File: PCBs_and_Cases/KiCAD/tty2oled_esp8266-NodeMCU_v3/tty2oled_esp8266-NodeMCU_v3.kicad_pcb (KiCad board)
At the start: 2 copper layers, 35.6 x 99.7 mm, 2 parts

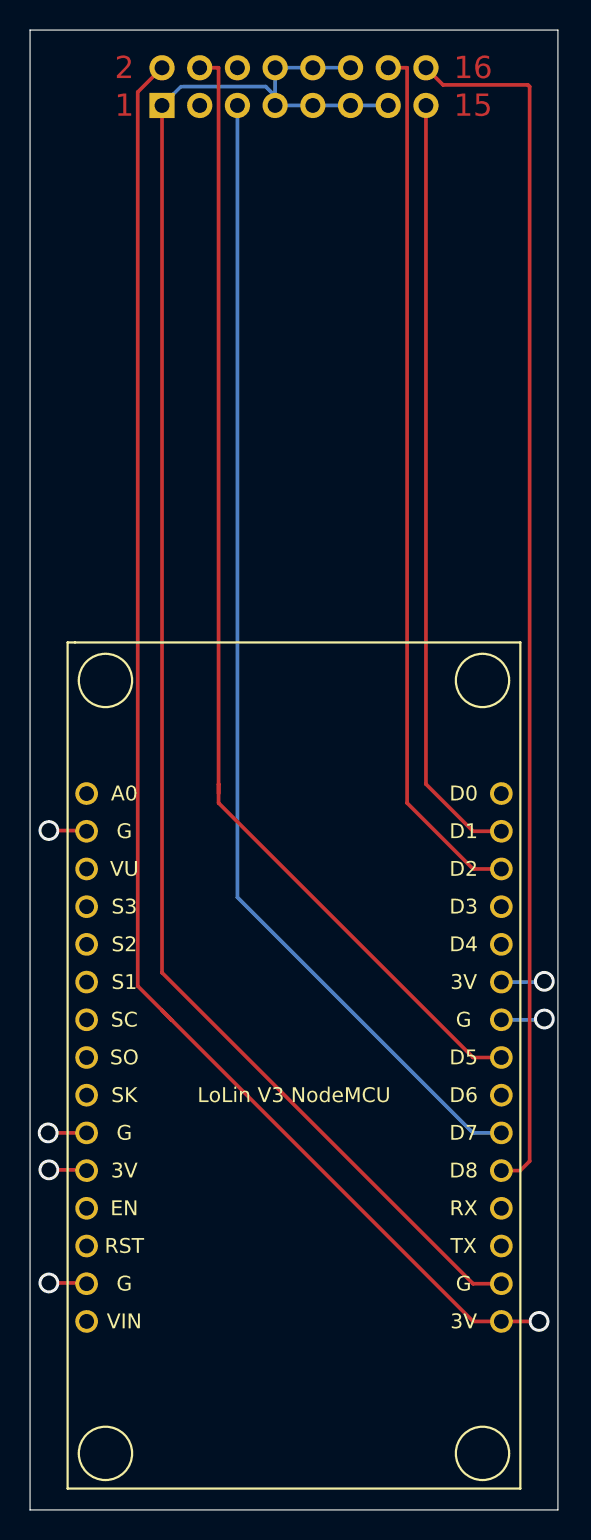
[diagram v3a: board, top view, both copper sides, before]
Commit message: Silkscreen fixed
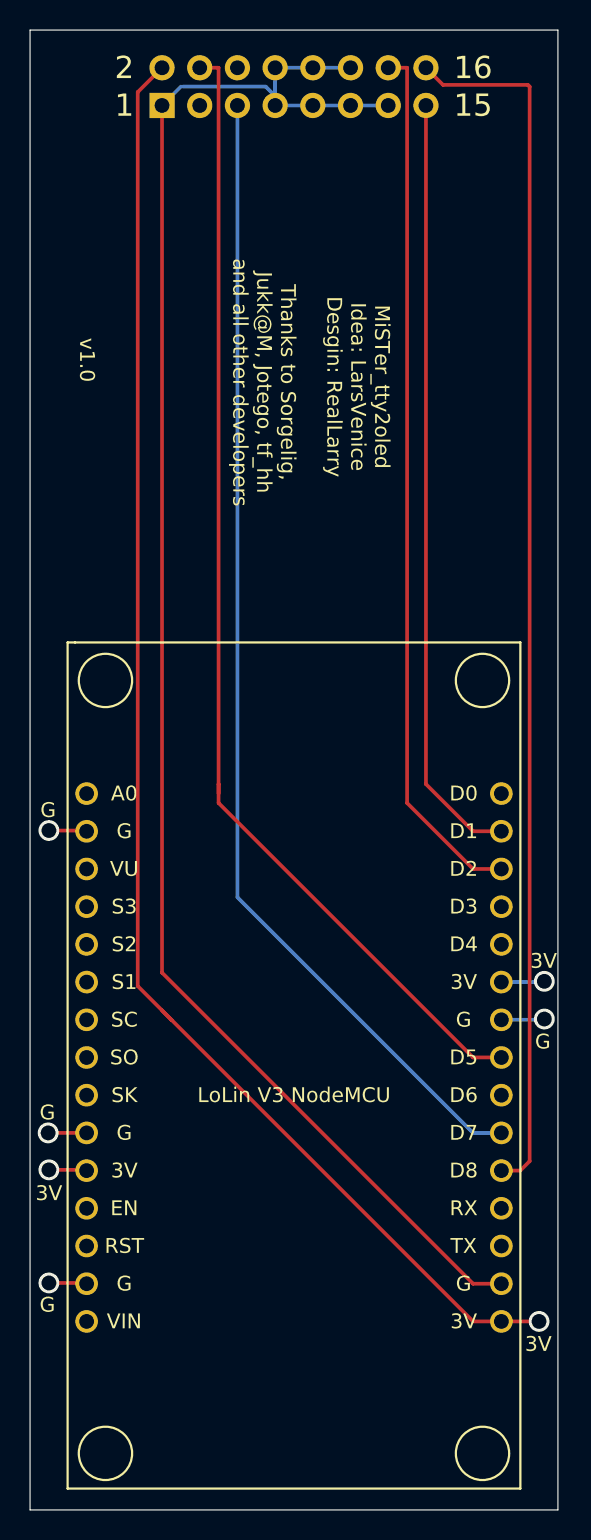
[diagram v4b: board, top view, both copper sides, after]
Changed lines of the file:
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@@
       (effects (font (size 1 1) (thickness 0.15)))
     )
+    (fp_circle (center 12.7 24.13) (end 13.97 22.86) (layer F.SilkS) (width 0.15))
+    (fp_circle (center -12.7 24.13) (end -11.43 22.86) (layer F.SilkS) (width 0.15))
+    (fp_circle (center -12.7 -27.94) (end -11.43 -29.21) (layer F.SilkS) (width 0.15))
+    (fp_circle (center 12.7 -27.94) (end 13.97 -29.21) (layer F.SilkS) (width 0.15))
+    (fp_line (start 15.25 -30.5) (end -14.75 -30.5) (layer F.SilkS) (width 0.15))
+    (fp_line (start -14.75 -30.5) (end -15.25 -30.5) (layer F.SilkS) (width 0.15))
+    (fp_line (start -15.25 -30.5) (end -15.25 26.5) (layer F.SilkS) (width 0.15))
+    (fp_line (start -15.25 26.5) (end 15.25 26.5) (layer F.SilkS) (width 0.15))
     (fp_line (start 15.25 26.5) (end 15.25 -30.5) (layer F.SilkS) (width 0.15))
-    (fp_line (start -15.25 26.5) (end 15.25 26.5) (layer F.SilkS) (width 0.15))
-    (fp_line (start -15.25 -30.5) (end -15.25 26.5) (layer F.SilkS) (width 0.15))
-    (fp_line (start -14.75 -30.5) (end -15.25 -30.5) (layer F.SilkS) (width 0.15))
-    (fp_line (start 15.25 -30.5) (end -14.75 -30.5) (layer F.SilkS) (width 0.15))
-    (fp_circle (center 12.7 -27.94) (end 13.97 -29.21) (layer F.SilkS) (width 0.15))
-    (fp_circle (center -12.7 -27.94) (end -11.43 -29.21) (layer F.SilkS) (width 0.15))
-    (fp_circle (center -12.7 24.13) (end -11.43 22.86) (layer F.SilkS) (width 0.15))
-    (fp_circle (center 12.7 24.13) (end 13.97 22.86) (layer F.SilkS) (width 0.15))
     (fp_text user D0 (at 11.43 -20.32) (layer F.SilkS)
       (effects (font (size 1 1) (thickness 0.15)))
@@
       (effects (font (size 1 1) (thickness 0.15)) (justify mirror))
     )
+    (fp_line (start 4.35 1.8) (end -1.8 1.8) (layer B.CrtYd) (width 0.05))
+    (fp_line (start 4.35 -19.55) (end 4.35 1.8) (layer B.CrtYd) (width 0.05))
+    (fp_line (start -1.8 -19.55) (end 4.35 -19.55) (layer B.CrtYd) (width 0.05))
+    (fp_line (start -1.8 1.8) (end -1.8 -19.55) (layer B.CrtYd) (width 0.05))
+    (fp_line (start -1.33 1.33) (end 0 1.33) (layer B.SilkS) (width 0.12))
+    (fp_line (start -1.33 0) (end -1.33 1.33) (layer B.SilkS) (width 0.12))
+    (fp_line (start 1.27 1.33) (end 3.87 1.33) (layer B.SilkS) (width 0.12))
+    (fp_line (start 1.27 -1.27) (end 1.27 1.33) (layer B.SilkS) (width 0.12))
+    (fp_line (start -1.33 -1.27) (end 1.27 -1.27) (layer B.SilkS) (width 0.12))
+    (fp_line (start 3.87 1.33) (end 3.87 -19.11) (layer B.SilkS) (width 0.12))
+    (fp_line (start -1.33 -1.27) (end -1.33 -19.11) (layer B.SilkS) (width 0.12))
+    (fp_line (start -1.33 -19.11) (end 3.87 -19.11) (layer B.SilkS) (width 0.12))
+    (fp_line (start -1.27 0) (end 0 1.27) (layer B.Fab) (width 0.1))
+    (fp_line (start -1.27 -19.05) (end -1.27 0) (layer B.Fab) (width 0.1))
+    (fp_line (start 3.81 -19.05) (end -1.27 -19.05) (layer B.Fab) (width 0.1))
+    (fp_line (start 3.81 1.27) (end 3.81 -19.05) (layer B.Fab) (width 0.1))
     (fp_line (start 0 1.27) (end 3.81 1.27) (layer B.Fab) (width 0.1))
-    (fp_line (start 3.81 1.27) (end 3.81 -19.05) (layer B.Fab) (width 0.1))
-    (fp_line (start 3.81 -19.05) (end -1.27 -19.05) (layer B.Fab) (width 0.1))
-    (fp_line (start -1.27 -19.05) (end -1.27 0) (layer B.Fab) (width 0.1))
-    (fp_line (start -1.27 0) (end 0 1.27) (layer B.Fab) (width 0.1))
-    (fp_line (start -1.33 -19.11) (end 3.87 -19.11) (layer B.SilkS) (width 0.12))
-    (fp_line (start -1.33 -1.27) (end -1.33 -19.11) (layer B.SilkS) (width 0.12))
-    (fp_line (start 3.87 1.33) (end 3.87 -19.11) (layer B.SilkS) (width 0.12))
-    (fp_line (start -1.33 -1.27) (end 1.27 -1.27) (layer B.SilkS) (width 0.12))
-    (fp_line (start 1.27 -1.27) (end 1.27 1.33) (layer B.SilkS) (width 0.12))
-    (fp_line (start 1.27 1.33) (end 3.87 1.33) (layer B.SilkS) (width 0.12))
-    (fp_line (start -1.33 0) (end -1.33 1.33) (layer B.SilkS) (width 0.12))
-    (fp_line (start -1.33 1.33) (end 0 1.33) (layer B.SilkS) (width 0.12))
-    (fp_line (start -1.8 1.8) (end -1.8 -19.55) (layer B.CrtYd) (width 0.05))
-    (fp_line (start -1.8 -19.55) (end 4.35 -19.55) (layer B.CrtYd) (width 0.05))
-    (fp_line (start 4.35 -19.55) (end 4.35 1.8) (layer B.CrtYd) (width 0.05))
-    (fp_line (start 4.35 1.8) (end -1.8 1.8) (layer B.CrtYd) (width 0.05))
     (fp_text user %R (at 1.27 -8.89 180) (layer B.Fab)
       (effects (font (size 1 1) (thickness 0.15)) (justify mirror))
@@
     )
   )
-  (gr_text G (at 133.2484 137.3124) (layer F.Paste)
-    (effects (font (size 1 1) (thickness 0.15)))
-  )
-  (gr_text 3V (at 133.35 129.794) (layer F.Paste)
-    (effects (font (size 1 1) (thickness 0.15)))
-  )
-  (gr_text G (at 133.2484 124.3584) (layer F.Paste)
-    (effects (font (size 1 1) (thickness 0.15)))
-  )
-  (gr_text G (at 133.2992 103.9876) (layer F.Paste)
-    (effects (font (size 1 1) (thickness 0.15)))
-  )
-  (gr_text 3V (at 166.6748 114.1476) (layer F.Paste)
-    (effects (font (size 1 1) (thickness 0.15)))
-  )
-  (gr_text G (at 166.624 119.5832) (layer F.Paste)
-    (effects (font (size 1 1) (thickness 0.15)))
-  )
-  (gr_text 3V (at 166.3192 139.954) (layer F.Paste)
-    (effects (font (size 1 1) (thickness 0.15)))
-  )
-  (gr_text v1.0 (at 135.9154 73.66 -90) (layer F.Paste)
-    (effects (font (size 1 1) (thickness 0.15)))
-  )
-  (gr_text "Thanks to Sorgelig,\nJukk@M, Jotego, tf_hh\nand all other developers" (at 147.8407 75.1713 -90) (layer F.Paste)
-    (effects (font (size 1 1) (thickness 0.15)))
-  )
-  (gr_text "MiSTer_tty2oled\nIdea: LarsVenice\nDesgin: RealLarry" (at 154.178 75.4634 -90) (layer F.Paste)
+  (gr_text G (at 133.2484 137.3124) (layer F.SilkS)
+    (effects (font (size 1 1) (thickness 0.15)))
+  )
+  (gr_text 3V (at 133.35 129.794) (layer F.SilkS)
+    (effects (font (size 1 1) (thickness 0.15)))
+  )
+  (gr_text G (at 133.2484 124.3584) (layer F.SilkS)
+    (effects (font (size 1 1) (thickness 0.15)))
+  )
+  (gr_text G (at 133.2992 103.9876) (layer F.SilkS)
+    (effects (font (size 1 1) (thickness 0.15)))
+  )
+  (gr_text 3V (at 166.6748 114.1476) (layer F.SilkS)
+    (effects (font (size 1 1) (thickness 0.15)))
+  )
+  (gr_text G (at 166.624 119.5832) (layer F.SilkS)
+    (effects (font (size 1 1) (thickness 0.15)))
+  )
+  (gr_text 3V (at 166.3192 139.954) (layer F.SilkS)
+    (effects (font (size 1 1) (thickness 0.15)))
+  )
+  (gr_text v1.0 (at 135.9154 73.66 -90) (layer F.SilkS)
+    (effects (font (size 1 1) (thickness 0.15)))
+  )
+  (gr_text "Thanks to Sorgelig,\nJukk@M, Jotego, tf_hh\nand all other developers" (at 147.8407 75.1713 -90) (layer F.SilkS)
+    (effects (font (size 1 1) (thickness 0.15)))
+  )
+  (gr_text "MiSTer_tty2oled\nIdea: LarsVenice\nDesgin: RealLarry" (at 154.178 75.4634 -90) (layer F.SilkS)
     (effects (font (size 1 1) (thickness 0.15)))
   )
@@
   (gr_line (start 132.08 151.13) (end 167.64 151.13) (layer Edge.Cuts) (width 0.05))
   (target plus (at 109.855 91.44) (size 5) (width 0.05) (layer Edge.Cuts))
-  (gr_text 16 (at 161.925 53.975) (layer F.Cu)
-    (effects (font (size 1.5 1.5) (thickness 0.3)))
-  )
-  (gr_text 15 (at 161.925 56.515) (layer F.Cu)
-    (effects (font (size 1.5 1.5) (thickness 0.3)))
-  )
-  (gr_text 2 (at 138.43 53.975) (layer F.Cu)
-    (effects (font (size 1.5 1.5) (thickness 0.3)))
-  )
-  (gr_text 1 (at 138.43 56.515) (layer F.Cu)
-    (effects (font (size 1.5 1.5) (thickness 0.3)))
-  )
+  (gr_text 16 (at 161.925 53.975) (layer F.SilkS)
+    (effects (font (size 1.5 1.5) (thickness 0.3)))
+  )
+  (gr_text 15 (at 161.925 56.515) (layer F.SilkS)
+    (effects (font (size 1.5 1.5) (thickness 0.3)))
+  )
+  (gr_text 2 (at 138.43 53.975) (layer F.SilkS)
+    (effects (font (size 1.5 1.5) (thickness 0.3)))
+  )
+  (gr_text 1 (at 138.43 56.515) (layer F.SilkS)
+    (effects (font (size 1.5 1.5) (thickness 0.3)))
+  )

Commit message: Update board esp8266 to v1.1
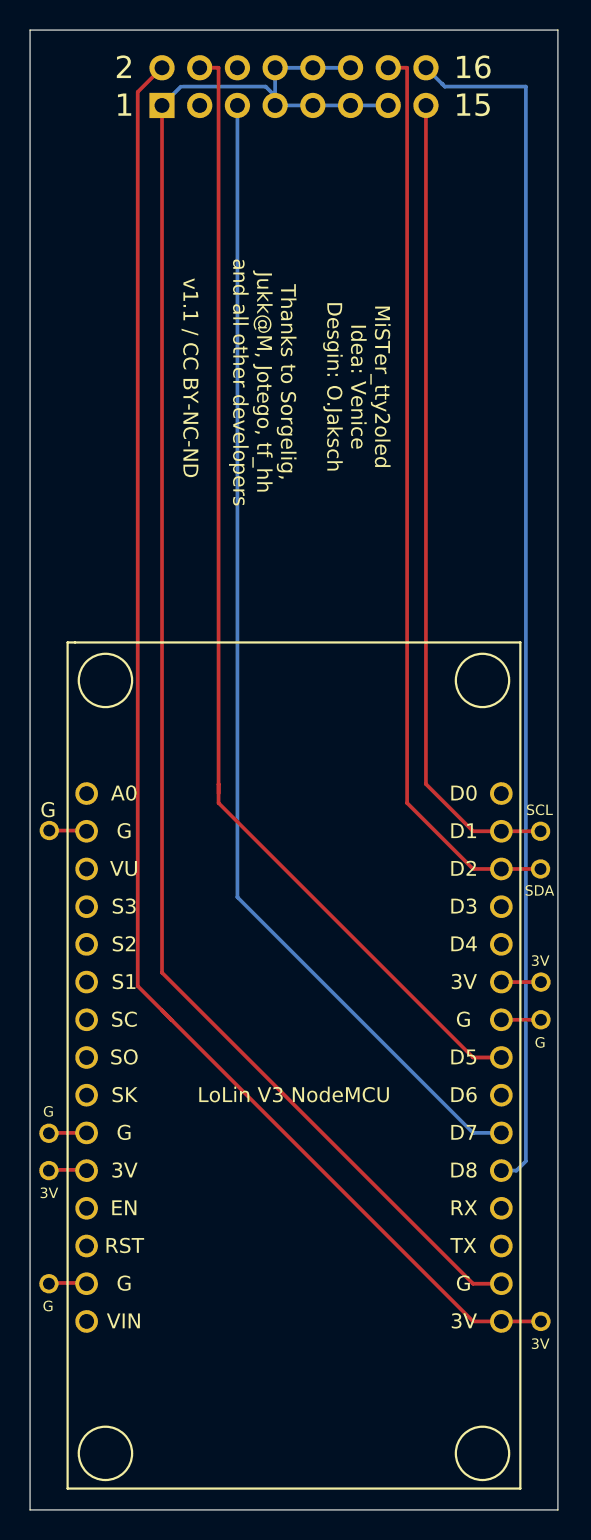
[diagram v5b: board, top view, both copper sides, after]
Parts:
- added REF**: SolderWirePad_single_0-8mmDrill, Wire_Pads:SolderWirePad_single_0-8mmDrill, F.Cu at (166.5, 108.0)
- added REF**: SolderWirePad_single_0-8mmDrill, Wire_Pads:SolderWirePad_single_0-8mmDrill, F.Cu at (166.5, 105.4)
- added REF**: SolderWirePad_single_0-8mmDrill, Wire_Pads:SolderWirePad_single_0-8mmDrill, F.Cu at (133.3, 135.9)
- added REF**: SolderWirePad_single_0-8mmDrill, Wire_Pads:SolderWirePad_single_0-8mmDrill, F.Cu at (133.3, 128.3)
- added REF**: SolderWirePad_single_0-8mmDrill, Wire_Pads:SolderWirePad_single_0-8mmDrill, F.Cu at (133.3, 125.8)
- added REF**: SolderWirePad_single_0-8mmDrill, Wire_Pads:SolderWirePad_single_0-8mmDrill, F.Cu at (133.4, 105.4)
- added REF**: SolderWirePad_single_0-8mmDrill, Wire_Pads:SolderWirePad_single_0-8mmDrill, F.Cu at (166.5, 138.4)
- added REF**: SolderWirePad_single_0-8mmDrill, Wire_Pads:SolderWirePad_single_0-8mmDrill, F.Cu at (166.5, 115.6)
- added REF**: SolderWirePad_single_0-8mmDrill, Wire_Pads:SolderWirePad_single_0-8mmDrill, F.Cu at (166.5, 118.1)
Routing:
- net (no net): track 579.2 -> 583.9 mm, vias 7 -> 0
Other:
- board text added: "MiSTer_tty2oled Idea: Venice Desgin: O.Jaksch"
- board text added: "SCL"
- board text added: "SDA"
- board text added: "v1.1 / CC BY-NC-ND"
- board text removed: "MiSTer_tty2oled Idea: LarsVenice Desgin: RealLarry"
- board text removed: "v1.0"

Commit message: Fixup of license esp8266
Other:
- board text added: "v1.1 / CC BY-NC-SA"
- board text removed: "v1.1 / CC BY-NC-ND"
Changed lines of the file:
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@@
       (effects (font (size 1 1) (thickness 0.15)))
     )
+    (fp_line (start 15.25 26.5) (end 15.25 -30.5) (layer F.SilkS) (width 0.15))
+    (fp_line (start -15.25 26.5) (end 15.25 26.5) (layer F.SilkS) (width 0.15))
+    (fp_line (start -15.25 -30.5) (end -15.25 26.5) (layer F.SilkS) (width 0.15))
+    (fp_line (start -14.75 -30.5) (end -15.25 -30.5) (layer F.SilkS) (width 0.15))
+    (fp_line (start 15.25 -30.5) (end -14.75 -30.5) (layer F.SilkS) (width 0.15))
+    (fp_circle (center 12.7 -27.94) (end 13.97 -29.21) (layer F.SilkS) (width 0.15))
+    (fp_circle (center -12.7 -27.94) (end -11.43 -29.21) (layer F.SilkS) (width 0.15))
+    (fp_circle (center -12.7 24.13) (end -11.43 22.86) (layer F.SilkS) (width 0.15))
     (fp_circle (center 12.7 24.13) (end 13.97 22.86) (layer F.SilkS) (width 0.15))
-    (fp_circle (center -12.7 24.13) (end -11.43 22.86) (layer F.SilkS) (width 0.15))
-    (fp_circle (center -12.7 -27.94) (end -11.43 -29.21) (layer F.SilkS) (width 0.15))
-    (fp_circle (center 12.7 -27.94) (end 13.97 -29.21) (layer F.SilkS) (width 0.15))
-    (fp_line (start 15.25 -30.5) (end -14.75 -30.5) (layer F.SilkS) (width 0.15))
-    (fp_line (start -14.75 -30.5) (end -15.25 -30.5) (layer F.SilkS) (width 0.15))
-    (fp_line (start -15.25 -30.5) (end -15.25 26.5) (layer F.SilkS) (width 0.15))
-    (fp_line (start -15.25 26.5) (end 15.25 26.5) (layer F.SilkS) (width 0.15))
-    (fp_line (start 15.25 26.5) (end 15.25 -30.5) (layer F.SilkS) (width 0.15))
     (fp_text user D0 (at 11.43 -20.32) (layer F.SilkS)
       (effects (font (size 1 1) (thickness 0.15)))
@@
       (effects (font (size 1 1) (thickness 0.15)) (justify mirror))
     )
+    (fp_line (start 0 1.27) (end 3.81 1.27) (layer B.Fab) (width 0.1))
+    (fp_line (start 3.81 1.27) (end 3.81 -19.05) (layer B.Fab) (width 0.1))
+    (fp_line (start 3.81 -19.05) (end -1.27 -19.05) (layer B.Fab) (width 0.1))
+    (fp_line (start -1.27 -19.05) (end -1.27 0) (layer B.Fab) (width 0.1))
+    (fp_line (start -1.27 0) (end 0 1.27) (layer B.Fab) (width 0.1))
+    (fp_line (start -1.33 -19.11) (end 3.87 -19.11) (layer B.SilkS) (width 0.12))
+    (fp_line (start -1.33 -1.27) (end -1.33 -19.11) (layer B.SilkS) (width 0.12))
+    (fp_line (start 3.87 1.33) (end 3.87 -19.11) (layer B.SilkS) (width 0.12))
+    (fp_line (start -1.33 -1.27) (end 1.27 -1.27) (layer B.SilkS) (width 0.12))
+    (fp_line (start 1.27 -1.27) (end 1.27 1.33) (layer B.SilkS) (width 0.12))
+    (fp_line (start 1.27 1.33) (end 3.87 1.33) (layer B.SilkS) (width 0.12))
+    (fp_line (start -1.33 0) (end -1.33 1.33) (layer B.SilkS) (width 0.12))
+    (fp_line (start -1.33 1.33) (end 0 1.33) (layer B.SilkS) (width 0.12))
+    (fp_line (start -1.8 1.8) (end -1.8 -19.55) (layer B.CrtYd) (width 0.05))
+    (fp_line (start -1.8 -19.55) (end 4.35 -19.55) (layer B.CrtYd) (width 0.05))
+    (fp_line (start 4.35 -19.55) (end 4.35 1.8) (layer B.CrtYd) (width 0.05))
     (fp_line (start 4.35 1.8) (end -1.8 1.8) (layer B.CrtYd) (width 0.05))
-    (fp_line (start 4.35 -19.55) (end 4.35 1.8) (layer B.CrtYd) (width 0.05))
-    (fp_line (start -1.8 -19.55) (end 4.35 -19.55) (layer B.CrtYd) (width 0.05))
-    (fp_line (start -1.8 1.8) (end -1.8 -19.55) (layer B.CrtYd) (width 0.05))
-    (fp_line (start -1.33 1.33) (end 0 1.33) (layer B.SilkS) (width 0.12))
-    (fp_line (start -1.33 0) (end -1.33 1.33) (layer B.SilkS) (width 0.12))
-    (fp_line (start 1.27 1.33) (end 3.87 1.33) (layer B.SilkS) (width 0.12))
-    (fp_line (start 1.27 -1.27) (end 1.27 1.33) (layer B.SilkS) (width 0.12))
-    (fp_line (start -1.33 -1.27) (end 1.27 -1.27) (layer B.SilkS) (width 0.12))
-    (fp_line (start 3.87 1.33) (end 3.87 -19.11) (layer B.SilkS) (width 0.12))
-    (fp_line (start -1.33 -1.27) (end -1.33 -19.11) (layer B.SilkS) (width 0.12))
-    (fp_line (start -1.33 -19.11) (end 3.87 -19.11) (layer B.SilkS) (width 0.12))
-    (fp_line (start -1.27 0) (end 0 1.27) (layer B.Fab) (width 0.1))
-    (fp_line (start -1.27 -19.05) (end -1.27 0) (layer B.Fab) (width 0.1))
-    (fp_line (start 3.81 -19.05) (end -1.27 -19.05) (layer B.Fab) (width 0.1))
-    (fp_line (start 3.81 1.27) (end 3.81 -19.05) (layer B.Fab) (width 0.1))
-    (fp_line (start 0 1.27) (end 3.81 1.27) (layer B.Fab) (width 0.1))
     (fp_text user %R (at 1.27 -8.89 180) (layer B.Fab)
       (effects (font (size 1 1) (thickness 0.15)) (justify mirror))
@@
     (effects (font (size 0.7 0.7) (thickness 0.15)))
   )
-  (gr_text "v1.1 / CC BY-NC-ND" (at 142.875 74.8792 -90) (layer F.SilkS)
+  (gr_text "v1.1 / CC BY-NC-SA" (at 142.875 74.8792 -90) (layer F.SilkS)
     (effects (font (size 1 1) (thickness 0.15)))
   )
